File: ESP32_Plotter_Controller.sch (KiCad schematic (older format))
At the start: 51 parts, among them J1 ARM JTAG 10pin, J10 Pen Lift, J11 Vselect, J12 X Motor, J13 Y Motor, J14 Neo Pixel LEDs, J15 Pen Direction, J16 Aux Port (I2C), J17 USB_C_Receptacle_USB2.0, J18 E-Stop, J19 Y Limit Switch, J2 Power, J3 5V Aux, J4 Vin Aux, J5 X Limit Switch, J6 Aux Port (SPI), J7 X Limit, J8 Micro_SD_Card_TF-01A, J9 Y Limit, SW1 RESET, SW2 BOOT, U1 ESP32-WROOM-32D, U2 TMC2130, U3 TMC2130, U4 XL1509, U5 CH340C, U6 AMS1117-3.3

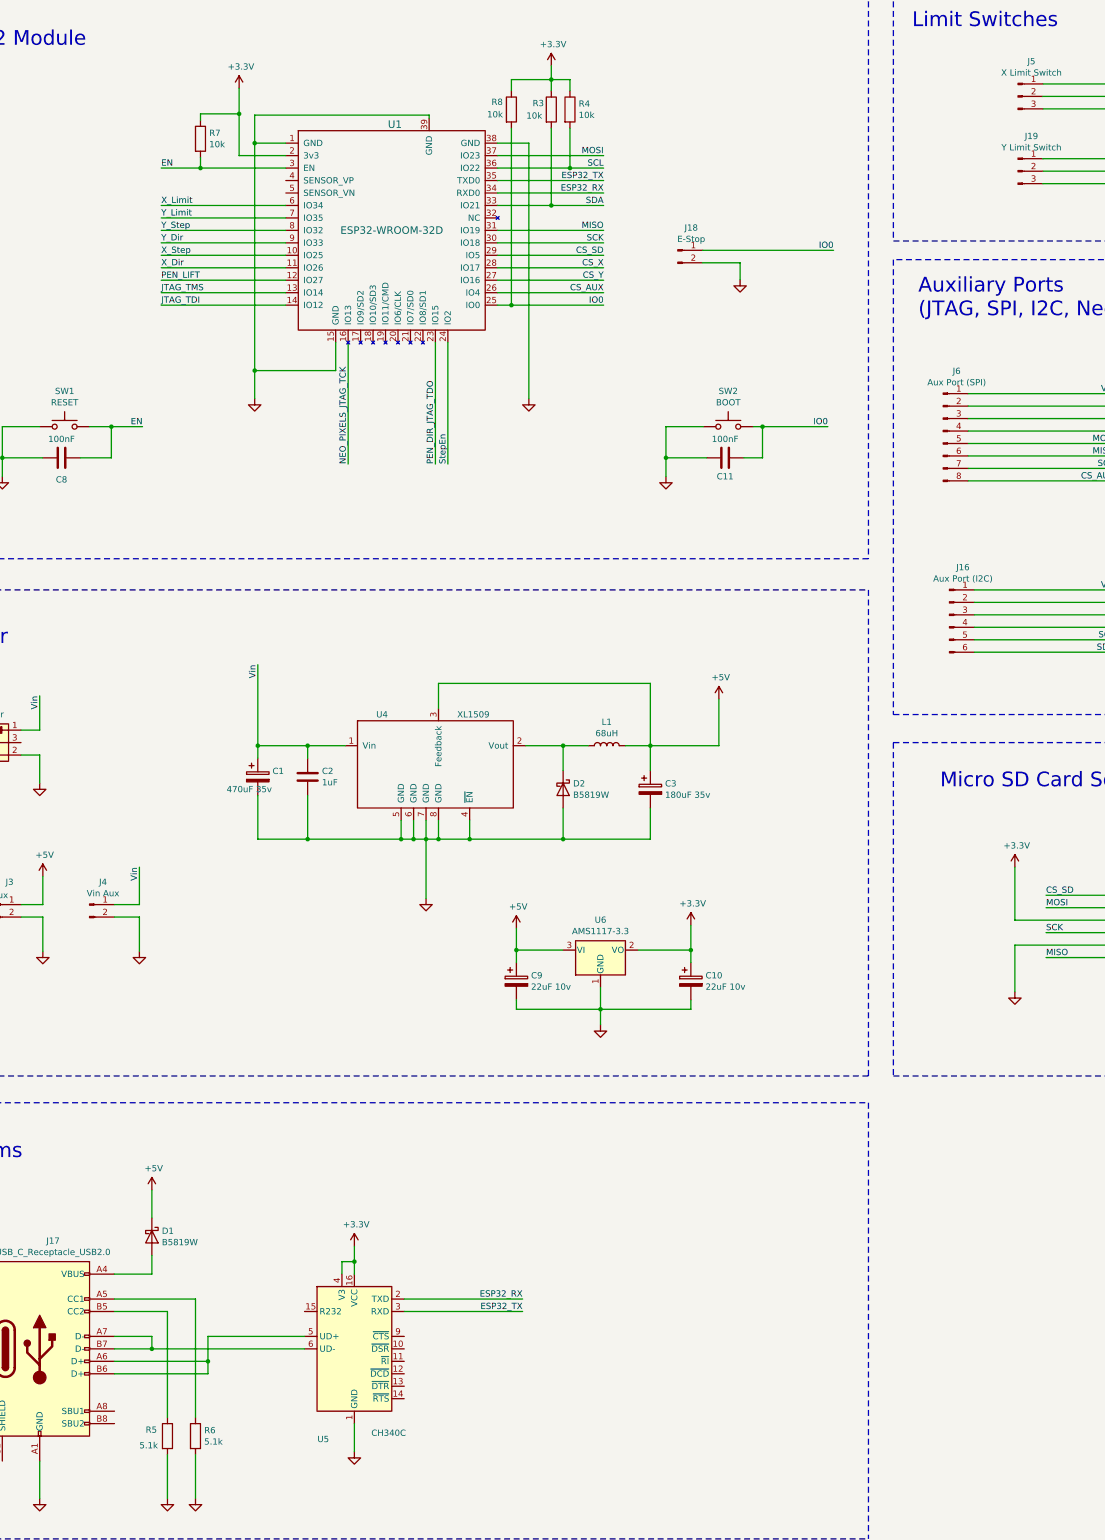
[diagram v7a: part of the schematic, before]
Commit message: Add decoupling capacitors
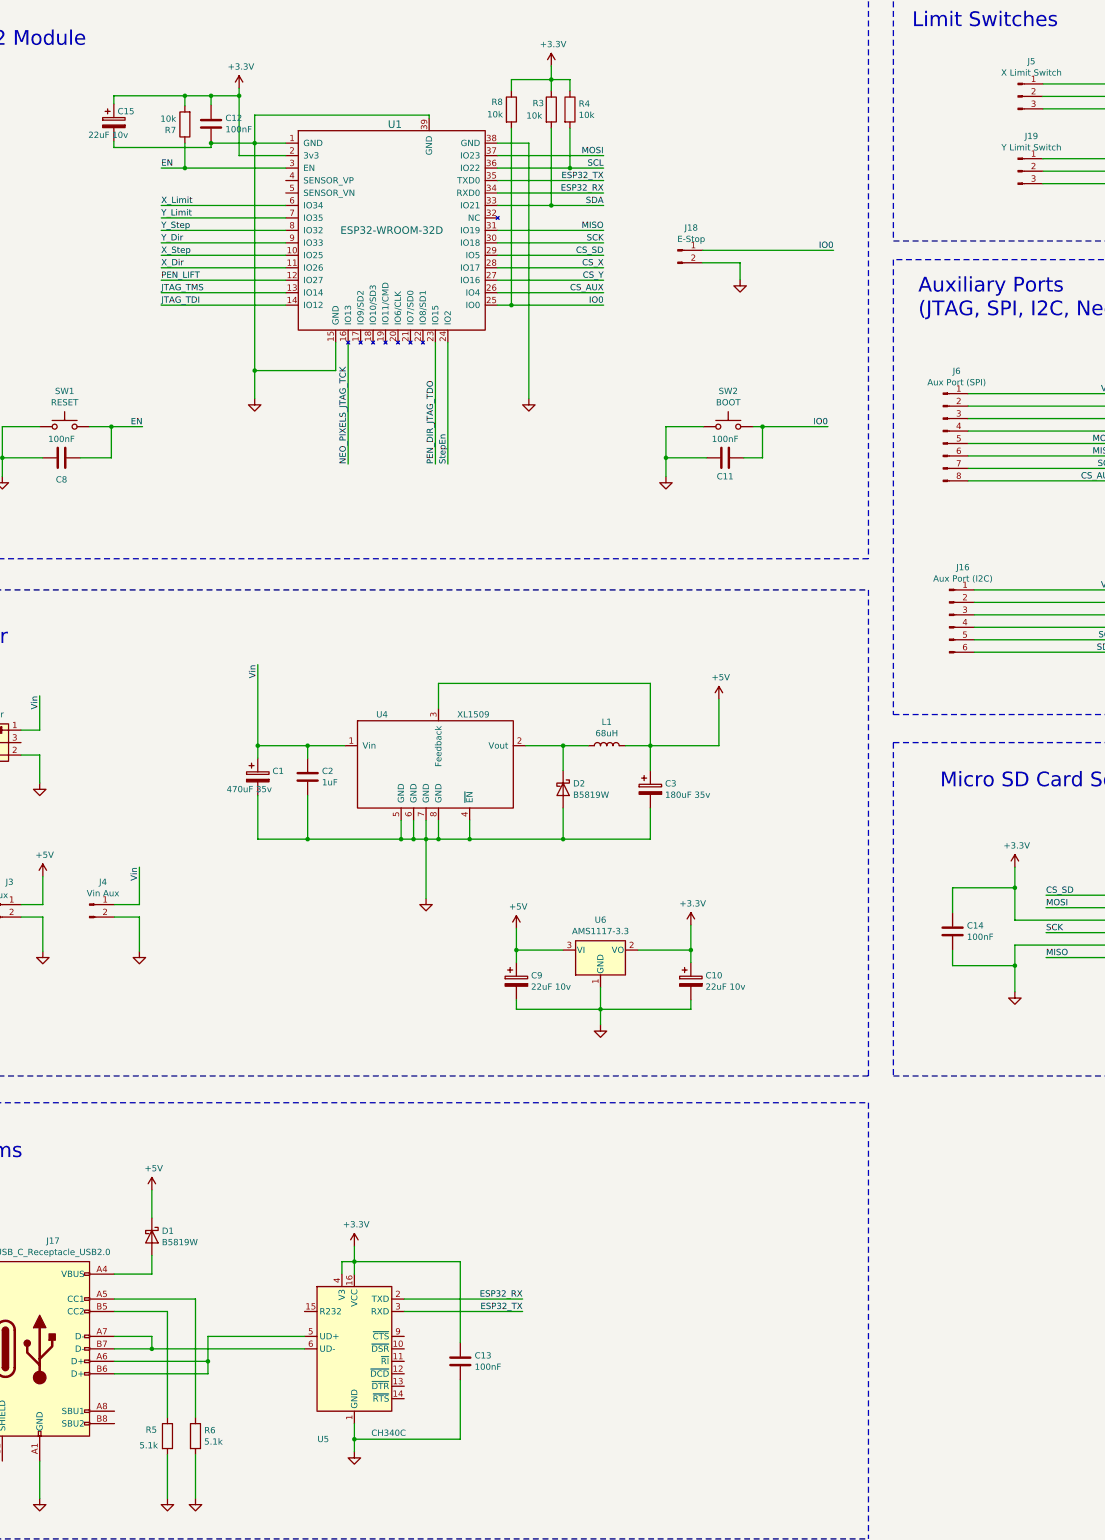
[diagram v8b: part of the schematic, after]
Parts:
- added C12, C13, C14: 100nF, Capacitor_SMD:C_0603_1608Metric, symbol Device:C
- added C15: 22uF 10v, Capacitor_Tantalum_SMD:CP_EIA-3216-18_Kemet-A, symbol Device:CP
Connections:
- net +3V3: now also R7.2, C12.1, C13.1, C14.1, C15.1; no longer R7.1
- net EN: now also R7.1; no longer R7.2
- net GND: now also C12.2, C13.2, C14.2, C15.2
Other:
- moved on the sheet: R7
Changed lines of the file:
@@
 $EndComp
 Wire Wire Line
-	9625 8210 9625 7785
+	9625 8210 9625 7950
 Wire Wire Line
 	9625 8210 10650 8210
@@
 $EndComp
 Wire Wire Line
-	9625 8410 9625 8785
+	9625 8410 9625 8575
 Wire Wire Line
 	9625 8410 10650 8410
@@
 	6055 2175 6325 2175
 Wire Wire Line
-	3525 1975 3775 1975
-Wire Wire Line
 	3400 2075 3775 2075
 Wire Wire Line
@@
 $EndComp
 Wire Wire Line
-	4325 12250 4325 12475
+	4325 12250 4325 12375
 $Comp
 L power:GND #NetPort07
@@
 	7600 4250 8125 4250
 Wire Wire Line
-	3775 2175 3090 2175
-Wire Wire Line
 	5475 3275 5585 3275
 Text Label 6325 3275 2    50   ~ 0
@@
 L Device:R R7
 U 1 1 61DBB1E2
-P 3090 1940
-F 0 "R7" H 3160 1986 50  0000 L CNN
-F 1 "10k" H 3160 1895 50  0000 L CNN
-F 2 "Resistor_SMD:R_0603_1608Metric" V 3020 1940 50  0001 C CNN
-F 3 "~" H 3090 1940 50  0001 C CNN
-	1    3090 1940
-	1    0    0    -1
+P 2965 1825
+F 0 "R7" H 3035 1871 50  0000 L CNN
+F 1 "10k" H 3035 1780 50  0000 L CNN
+F 2 "Resistor_SMD:R_0603_1608Metric" V 2895 1825 50  0001 C CNN
+F 3 "~" H 2965 1825 50  0001 C CNN
+	1    2965 1825
+	-1   0    0    1
 $EndComp
 $Comp
@@
 Wire Wire Line
 	5585 3275 6325 3275
-Wire Wire Line
-	3090 2090 3090 2175
-Connection ~ 3090 2175
-Wire Wire Line
-	3090 2175 2775 2175
-Wire Wire Line
-	3090 1740 3090 1790
-Wire Wire Line
-	3400 1535 3400 1740
-Wire Wire Line
-	3090 1740 3400 1740
-Connection ~ 3400 1740
-Wire Wire Line
-	3400 1740 3400 2075
 $Comp
 L Device:R R10
@@
 Wire Wire Line
 	15895 4210 16250 4210
+$Comp
+L Device:C C14
+U 1 1 61EEFA0E
+P 9125 8300
+F 0 "C14" H 9240 8346 50  0000 L CNN
+F 1 "100nF" H 9240 8255 50  0000 L CNN
+F 2 "Capacitor_SMD:C_0603_1608Metric" H 9163 8150 50  0001 C CNN
+F 3 "~" H 9125 8300 50  0001 C CNN
+	1    9125 8300
+	1    0    0    -1
+$EndComp
+Wire Wire Line
+	9125 8150 9125 7950
+Wire Wire Line
+	9125 7950 9625 7950
+Connection ~ 9625 7950
+Wire Wire Line
+	9625 7950 9625 7785
+Wire Wire Line
+	9125 8450 9125 8575
+Wire Wire Line
+	9125 8575 9625 8575
+Connection ~ 9625 8575
+Wire Wire Line
+	9625 8575 9625 8785
+$Comp
+L Device:C C13
+U 1 1 61F239D8
+P 5175 11750
+F 0 "C13" H 5290 11796 50  0000 L CNN
+F 1 "100nF" H 5290 11705 50  0000 L CNN
+F 2 "Capacitor_SMD:C_0603_1608Metric" H 5213 11600 50  0001 C CNN
+F 3 "~" H 5175 11750 50  0001 C CNN
+	1    5175 11750
+	1    0    0    -1
+$EndComp
+Wire Wire Line
+	5175 11600 5175 10950
+Wire Wire Line
+	5175 10950 4325 10950
+Wire Wire Line
+	4325 12375 5175 12375
+Wire Wire Line
+	5175 12375 5175 11900
+Connection ~ 4325 12375
+Wire Wire Line
+	4325 12375 4325 12475
+$Comp
+L Device:C C12
+U 1 1 61F591BC
+P 3175 1820
+F 0 "C12" H 3290 1866 50  0000 L CNN
+F 1 "100nF" H 3290 1775 50  0000 L CNN
+F 2 "Capacitor_SMD:C_0603_1608Metric" H 3213 1670 50  0001 C CNN
+F 3 "~" H 3175 1820 50  0001 C CNN
+	1    3175 1820
+	1    0    0    -1
+$EndComp
+Wire Wire Line
+	3525 1975 3775 1975
+Wire Wire Line
+	3400 1535 3400 1595
+Wire Wire Line
+	2775 2175 2965 2175
+Wire Wire Line
+	3175 1670 3175 1595
+Wire Wire Line
+	3175 1595 3400 1595
+Connection ~ 3400 1595
+Wire Wire Line
+	3400 1595 3400 2075
+Wire Wire Line
+	3175 1970 3175 1975
+Wire Wire Line
+	3175 1975 3525 1975
+Wire Wire Line
+	2965 1975 2965 2175
+Connection ~ 2965 2175
+Wire Wire Line
+	2965 2175 3775 2175
+Wire Wire Line
+	2965 1675 2965 1595
+Wire Wire Line
+	2965 1595 3175 1595
+Connection ~ 3175 1595
+$Comp
+L Device:CP C15
+U 1 1 6200B006
+P 2395 1810
+F 0 "C15" H 2425 1900 50  0000 L CNN
+F 1 "22uF 10v" H 2190 1710 50  0000 L CNN
+F 2 "Capacitor_Tantalum_SMD:CP_EIA-3216-18_Kemet-A" H 2433 1660 50  0001 C CNN
+F 3 "~" H 2395 1810 50  0001 C CNN
+	1    2395 1810
+	1    0    0    -1
+$EndComp
+Wire Wire Line
+	2965 1595 2395 1595
+Wire Wire Line
+	2395 1595 2395 1660
+Connection ~ 2965 1595
+Wire Wire Line
+	3175 1975 3175 2010
+Wire Wire Line
+	3175 2010 2395 2010
+Wire Wire Line
+	2395 2010 2395 1960
+Connection ~ 3175 1975
 $EndSCHEMATC
